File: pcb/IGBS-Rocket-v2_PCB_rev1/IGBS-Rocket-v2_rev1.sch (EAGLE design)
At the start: 269 parts, among them IC1 NCV21872DR2G, IC2 NCV21872DR2G, IC3 NCV21872DR2G, J1 U.FL, Q1 BC817, Q2 ENC-03, Q3 BSS316N, Q4 BC817, Q5 BSS314PE, U1 STM32H750VBT6, U10 24AA32A-I/ST, U11 u-blox NEO-M6, U2 LM317BD2TG, U3 CS5171EDR8G, U4 MPU-9250, U5 MICROSD, U6 ESP-12E/F, U7 BMP280, U8 LP324DRG4, U9 MCP6V51T-E/MS, Y1 24MHz

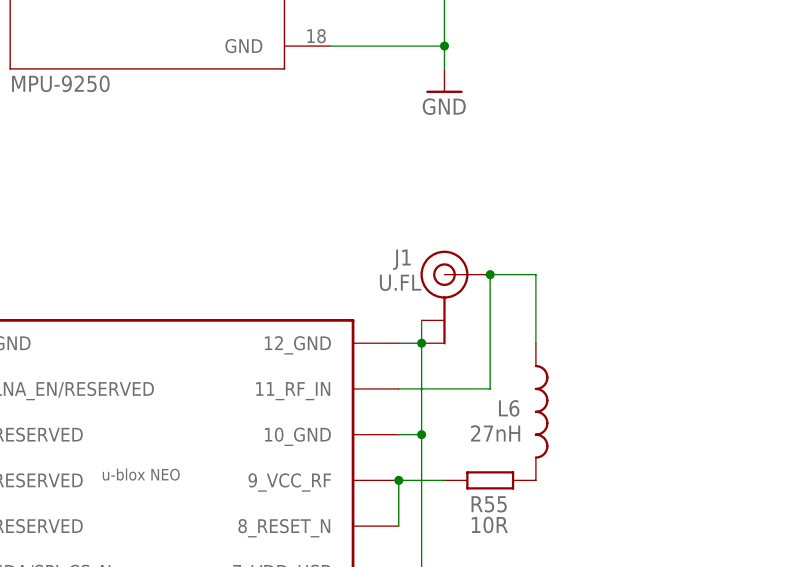
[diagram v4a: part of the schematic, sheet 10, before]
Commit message: + PCB layout check done (routing follows)
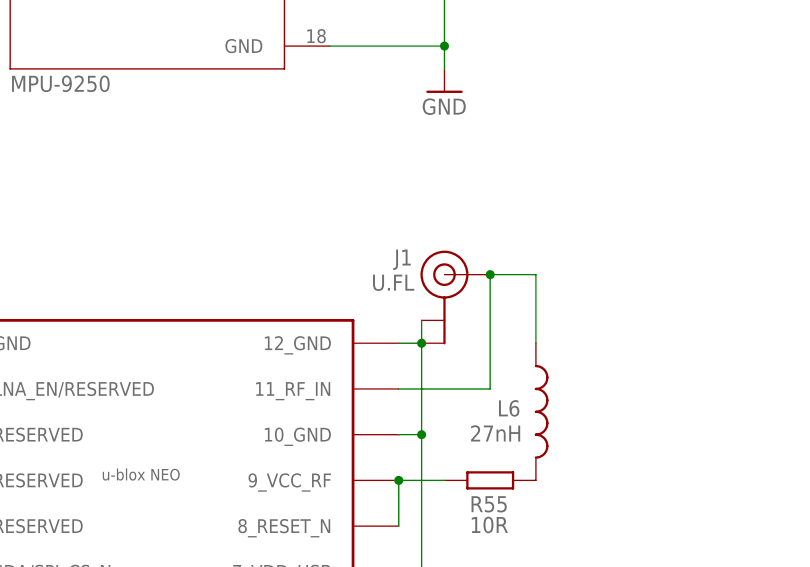
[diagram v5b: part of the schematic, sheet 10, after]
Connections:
- net N$27 renamed 12V-FB
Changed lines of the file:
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@@
 <drawing>
 <settings>
-<setting alwaysvectorfont="yes"/>
+<setting alwaysvectorfont="no"/>
 <setting verticaltext="up"/>
 </settings>
@@
 <part name="FRAME6" library="frames" library_urn="urn:adsk.eagle:library:229" deviceset="A4L-LOC" device=""/>
 <part name="FRAME7" library="frames" library_urn="urn:adsk.eagle:library:229" deviceset="A4L-LOC" device=""/>
-<part name="U1" library="stm" library_urn="urn:adsk.eagle:library:33748206" deviceset="STM32H750VBT6" device="LQFP100-14X14MM" package3d_urn="urn:adsk.eagle:package:33748214/3" value="STM32H750VBT6"/>
+<part name="U1" library="stm" library_urn="urn:adsk.eagle:library:33748206" deviceset="STM32H750VBT6" device="LQFP100-14X14MM" package3d_urn="urn:adsk.eagle:package:33748214/4" value="STM32H750VBT6"/>
 <part name="CR1" library="ldo" library_urn="urn:adsk.eagle:library:33748109" deviceset="LD1117DT50TR" device="" package3d_urn="urn:adsk.eagle:package:34444785/2" value="LD1117DT50"/>
 <part name="U5" library="microsd" library_urn="urn:adsk.eagle:library:33748539" deviceset="MICROSD-PUSH-OUT" device="" package3d_urn="urn:adsk.eagle:package:33748542/3" value="MICROSD"/>
-<part name="U6" library="esp-12e-f" library_urn="urn:adsk.eagle:library:33749161" deviceset="ESP-12E/F" device="" package3d_urn="urn:adsk.eagle:package:33749164/3"/>
+<part name="U6" library="esp-12e-f" library_urn="urn:adsk.eagle:library:33749161" deviceset="ESP-12E/F" device="" package3d_urn="urn:adsk.eagle:package:33749164/5"/>
 <part name="USB" library="usb" library_urn="urn:adsk.eagle:library:33767055" deviceset="USB-MINIB" device="-5PIN" package3d_urn="urn:adsk.eagle:package:33767058/3"/>
 <part name="PIANO" library="switch_btn" library_urn="urn:adsk.eagle:library:33768127" deviceset="A6FR-4101" device="SW_A6FR-4101_OMR" package3d_urn="urn:adsk.eagle:package:33768238/6"/>
@@
 <part name="Y1" library="SparkFun-Clocks" library_urn="urn:adsk.eagle:library:33781028" deviceset="OSCILLATOR-16MHZ" device="SMD-7X5-4PAD" package3d_urn="urn:adsk.eagle:package:33781096/3" value="24MHz"/>
 <part name="R1" library="rcl2" library_urn="urn:adsk.eagle:library:33772641" deviceset="R-EU_" device="R0603" package3d_urn="urn:adsk.eagle:package:33773532/5" value="150R"/>
-<part name="C6" library="rcl2" library_urn="urn:adsk.eagle:library:33772641" deviceset="CPOL-EU" device="CT3216" package3d_urn="urn:adsk.eagle:package:33773574/8" value="10u Tant"/>
+<part name="C6" library="rcl2" library_urn="urn:adsk.eagle:library:33772641" deviceset="CPOL-EU" device="CT3216" package3d_urn="urn:adsk.eagle:package:33773574/9" value="10u Tant"/>
 <part name="R2" library="rcl2" library_urn="urn:adsk.eagle:library:33772641" deviceset="R-EU_" device="R0603" package3d_urn="urn:adsk.eagle:package:33773532/5" value="560R"/>
 <part name="R3" library="rcl2" library_urn="urn:adsk.eagle:library:33772641" deviceset="R-EU_" device="R0603" package3d_urn="urn:adsk.eagle:package:33773532/5" value="1K8"/>
 <part name="R7" library="rcl2" library_urn="urn:adsk.eagle:library:33772641" deviceset="R-EU_" device="R0603" package3d_urn="urn:adsk.eagle:package:33773532/5" value="1K5"/>
-<part name="C10" library="rcl2" library_urn="urn:adsk.eagle:library:33772641" deviceset="CPOL-EU" device="CT3216" package3d_urn="urn:adsk.eagle:package:33773574/8" value="10u Tant"/>
+<part name="C10" library="rcl2" library_urn="urn:adsk.eagle:library:33772641" deviceset="CPOL-EU" device="CT3216" package3d_urn="urn:adsk.eagle:package:33773574/9" value="10u Tant"/>
 <part name="R8" library="rcl2" library_urn="urn:adsk.eagle:library:33772641" deviceset="R-EU_" device="R0603" package3d_urn="urn:adsk.eagle:package:33773532/5" value="240R"/>
 <part name="R9" library="rcl2" library_urn="urn:adsk.eagle:library:33772641" deviceset="R-EU_" device="R0603" package3d_urn="urn:adsk.eagle:package:33773532/5" value="390R"/>
@@
 </segment>
 </net>
-<net name="N$27" class="0">
+<net name="12V-FB" class="0">
 <segment>
 <pinref part="L5" gate="A" pin="1"/>
@@
 <instance part="J1" gate="G$1" x="132.08" y="99.06" smashed="yes">
 <attribute name="NAME" x="126.492" y="100.076" size="1.778" layer="95"/>
-<attribute name="VALUE" x="124.714" y="97.282" size="1.778" layer="95"/>
+<attribute name="VALUE" x="123.952" y="97.282" size="1.778" layer="95"/>
 </instance>
 <instance part="R99" gate="G$1" x="58.42" y="45.72" smashed="yes">

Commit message: * PCB routing 25 % done
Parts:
- added TP18: TPB1,27, testpad2:TPB1,27
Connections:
- net N$29 renamed 5V-BUZZER
- net N$39 renamed 5V-ESP
- net N$43 renamed 5V-MAG
- net N$76 renamed GPS-VBCKP2
- net BUZZER: now also TP18.TP

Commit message: + PCB routing signals 90 %
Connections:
- net 5V-ESP renamed 3V3-ESP
- removed net VCC: C54.1, L4.1, R44.2, R45.2, R46.2, R47.2, U10.VCC
- net 3V3: now also C54.1, L4.1, R44.2, R45.2, R46.2, R47.2, U10.VCC
